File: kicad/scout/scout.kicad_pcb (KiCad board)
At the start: 2 copper layers, 145.3 x 44.5 mm, 48 parts, among them J1 AudioJack2_SwitchT, J2 Conn_01x06_Male, J3 Conn_01x09, SW1 SW_SPST, SW10 SPST, SW11 SPST, SW12 SPST, SW13 SPST, SW14 SPST, SW15 SPST, SW16 SPST, SW17 SPST, SW18 SPST, SW2 SPST, SW3 SPST, SW4 SPST, SW5 SPST, SW6 SPST, SW7 SPST, SW8 SPST, SW9 SPST, U1 ATmega328P-PU, U2 LM386, Y1 16.00MHz

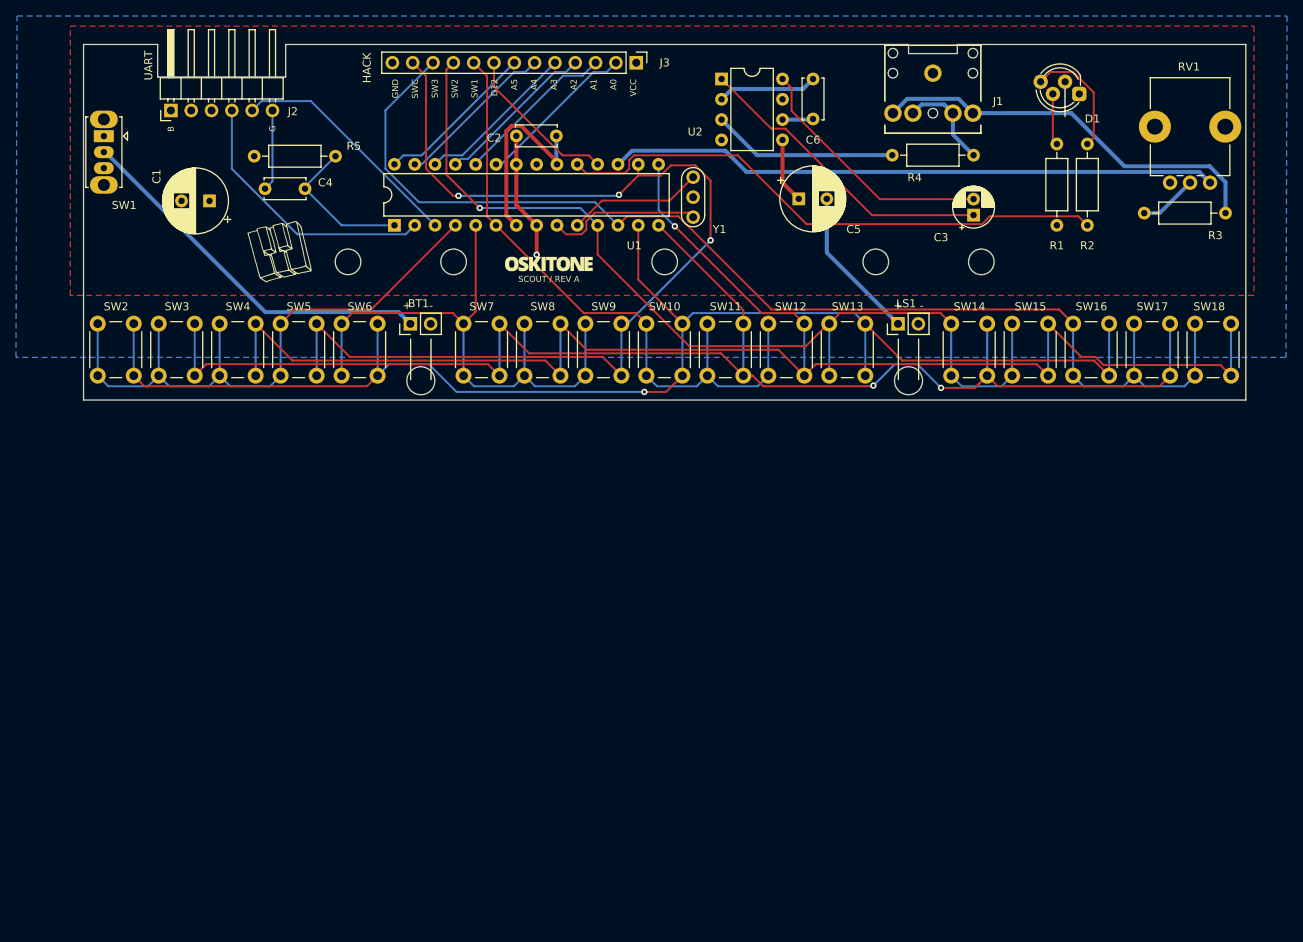
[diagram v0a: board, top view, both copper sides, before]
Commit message: Add diodes
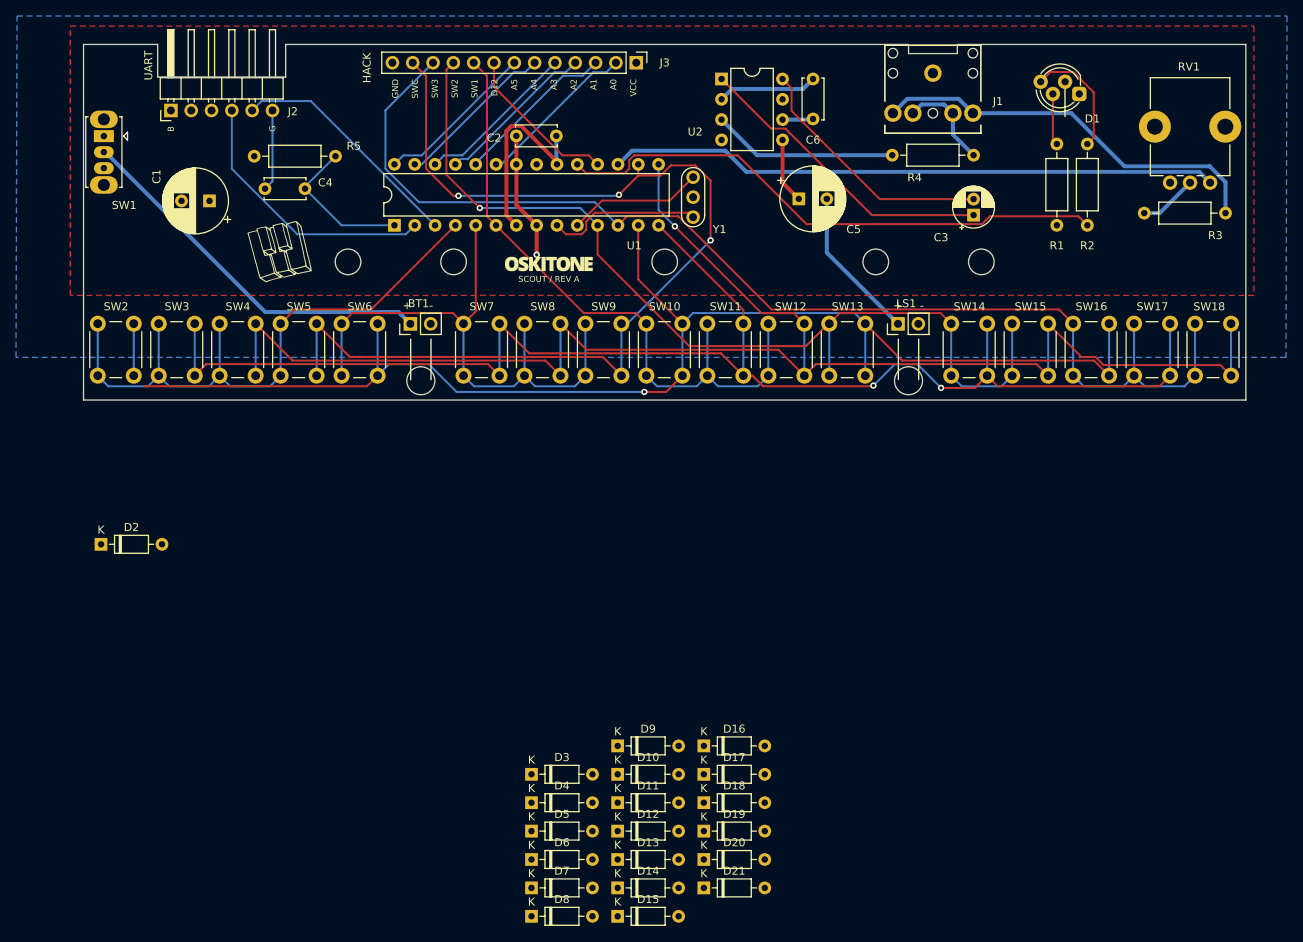
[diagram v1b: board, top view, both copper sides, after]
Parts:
- added D10: 1N4148, Diode_THT:D_DO-35_SOD27_P7.62mm_Horizontal, F.Cu at (98.8, 171.8)
- added D11: 1N4148, Diode_THT:D_DO-35_SOD27_P7.62mm_Horizontal, F.Cu at (98.8, 175.3)
- added D12: 1N4148, Diode_THT:D_DO-35_SOD27_P7.62mm_Horizontal, F.Cu at (98.8, 178.8)
- added D13: 1N4148, Diode_THT:D_DO-35_SOD27_P7.62mm_Horizontal, F.Cu at (98.8, 182.4)
- added D14: 1N4148, Diode_THT:D_DO-35_SOD27_P7.62mm_Horizontal, F.Cu at (98.8, 185.9)
- added D15: 1N4148, Diode_THT:D_DO-35_SOD27_P7.62mm_Horizontal, F.Cu at (98.8, 189.5)
- added D16: 1N4148, Diode_THT:D_DO-35_SOD27_P7.62mm_Horizontal, F.Cu at (109.5, 168.2)
- added D17: 1N4148, Diode_THT:D_DO-35_SOD27_P7.62mm_Horizontal, F.Cu at (109.5, 171.8)
- added D18: 1N4148, Diode_THT:D_DO-35_SOD27_P7.62mm_Horizontal, F.Cu at (109.5, 175.3)
- added D19: 1N4148, Diode_THT:D_DO-35_SOD27_P7.62mm_Horizontal, F.Cu at (109.5, 178.8)
- added D2: 1N4148, Diode_THT:D_DO-35_SOD27_P7.62mm_Horizontal, F.Cu at (34.2, 143.0)
- added D20: 1N4148, Diode_THT:D_DO-35_SOD27_P7.62mm_Horizontal, F.Cu at (109.5, 182.4)
- added D21: 1N4148, Diode_THT:D_DO-35_SOD27_P7.62mm_Horizontal, F.Cu at (109.5, 185.9)
- added D3: 1N4148, Diode_THT:D_DO-35_SOD27_P7.62mm_Horizontal, F.Cu at (88.0, 171.8)
- added D4: 1N4148, Diode_THT:D_DO-35_SOD27_P7.62mm_Horizontal, F.Cu at (88.0, 175.3)
- added D5: 1N4148, Diode_THT:D_DO-35_SOD27_P7.62mm_Horizontal, F.Cu at (88.0, 178.8)
- added D6: 1N4148, Diode_THT:D_DO-35_SOD27_P7.62mm_Horizontal, F.Cu at (88.0, 182.4)
- added D7: 1N4148, Diode_THT:D_DO-35_SOD27_P7.62mm_Horizontal, F.Cu at (88.0, 185.9)
- added D8: 1N4148, Diode_THT:D_DO-35_SOD27_P7.62mm_Horizontal, F.Cu at (88.0, 189.5)
- added D9: 1N4148, Diode_THT:D_DO-35_SOD27_P7.62mm_Horizontal, F.Cu at (98.8, 168.2)
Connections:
- D1 pad 1: (no net) -> unconnected-(D1-GA-Pad1)
- J3 pad 10: D5 -> /keyboard_matrix/SW2
- J3 pad 11: D6 -> /keyboard_matrix/SW3
- J3 pad 9: D4 -> /keyboard_matrix/SW1
- SW1 pad 3: (no net) -> unconnected-(SW1-C-Pad3)
- SW10 pad 2: D7 -> Net-(D10-K)
- SW11 pad 2: D8 -> Net-(D11-K)
- SW12 pad 2: D9 -> Net-(D12-K)
- SW13 pad 2: D7 -> Net-(D13-K)
- SW14 pad 2: D8 -> Net-(D14-K)
- SW15 pad 2: D9 -> Net-(D15-K)
- SW16 pad 2: D7 -> Net-(D16-K)
- SW17 pad 2: D8 -> Net-(D17-K)
- SW18 pad 2: D9 -> Net-(D18-K)
- SW2 pad 2: D7 -> Net-(D2-K)
- SW3 pad 2: D8 -> Net-(D3-K)
- SW4 pad 2: D9 -> Net-(D4-K)
- SW5 pad 2: D10 -> Net-(D5-K)
- SW6 pad 2: D7 -> Net-(D6-K)
- SW7 pad 2: D8 -> Net-(D7-K)
- SW8 pad 2: D9 -> Net-(D8-K)
- SW9 pad 2: D10 -> Net-(D9-K)
- U1 pad 21: (no net) -> unconnected-(U1-AREF-Pad21)
- U2 pad 7: (no net) -> unconnected-(U2-BYPASS-Pad7)
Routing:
- net D7: track 177.1 -> 168.7 mm
- net Net-(D2-K): track 0.00 -> 6.50 mm
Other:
- net class Default removed
